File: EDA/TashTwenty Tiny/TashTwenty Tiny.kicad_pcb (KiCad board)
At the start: 2 copper layers, 56.6 x 57.7 mm, 31 parts, among them J1 SD_Card, J2 IDC20, J3 Conn_01x02, Q1 BC337, U1 PIC16F1825-IP, U2 74ACT08, U3 MCP1700-3302E_TO92

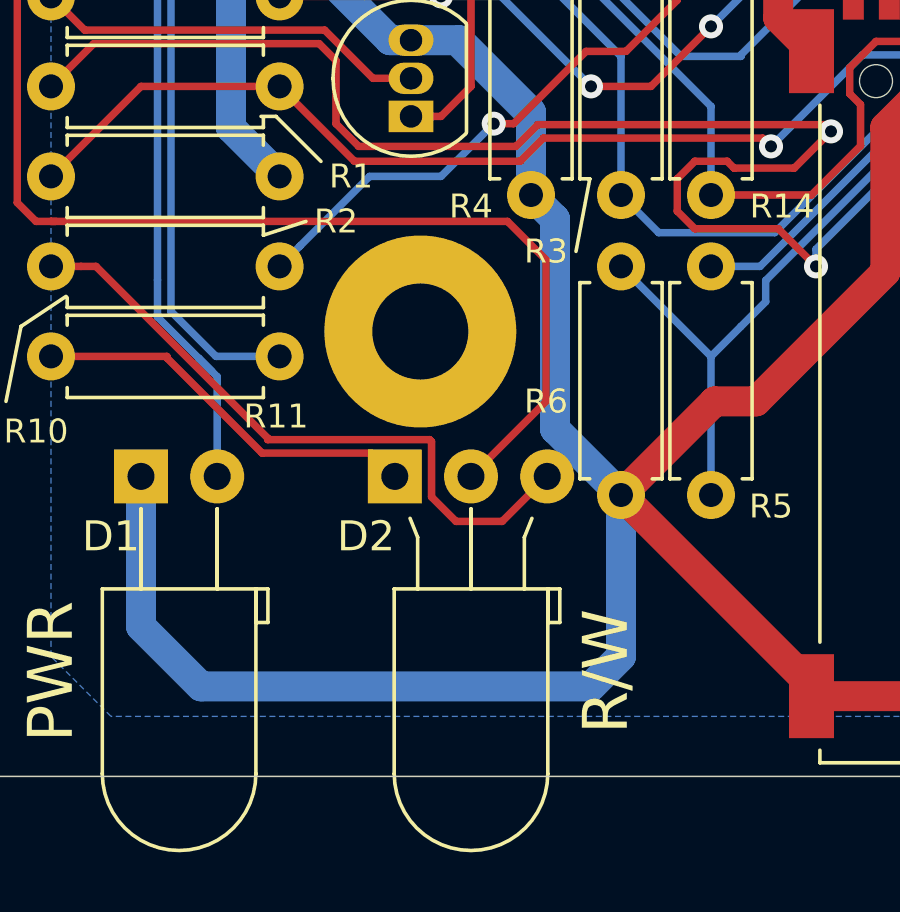
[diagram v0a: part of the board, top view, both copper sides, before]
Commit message: fixed DRC errors
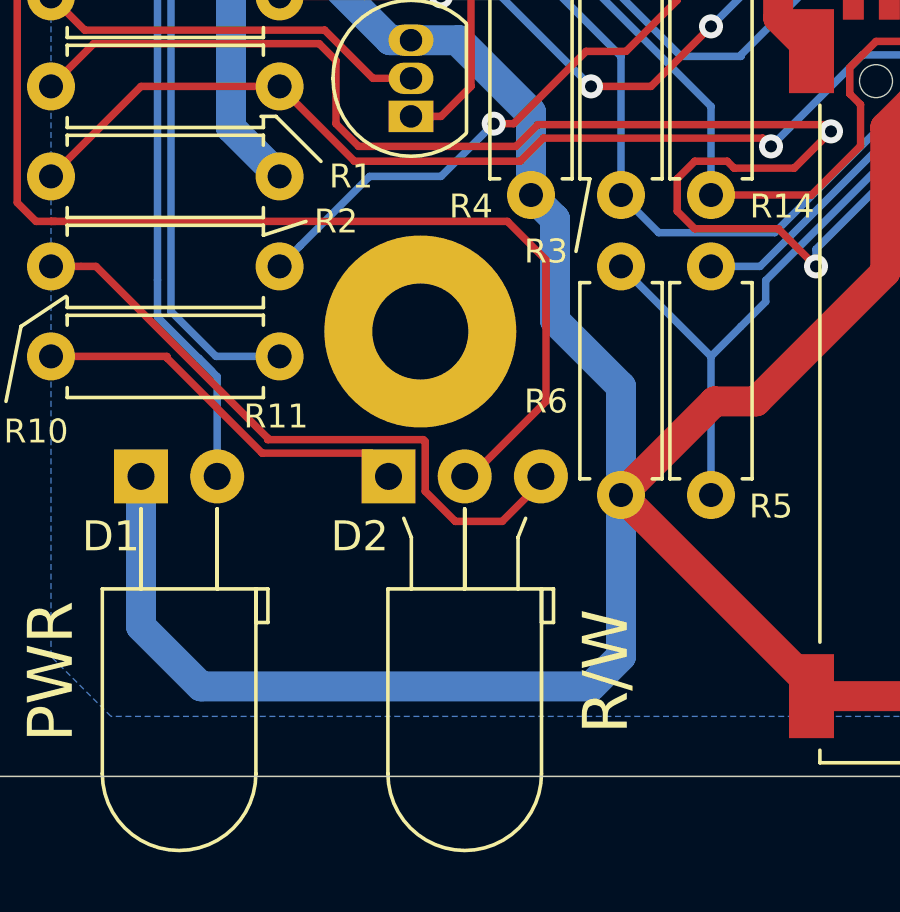
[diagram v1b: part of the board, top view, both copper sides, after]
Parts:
- moved D2 0.21 mm to (140.2, 117.0)
